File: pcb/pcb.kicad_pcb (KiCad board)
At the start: 2 copper layers, 63 x 56 mm, 70 parts, among them CN10 1x2, CN2 1x8, CN3 1x8, CN4 1x8, CN5 1x4, CN6 1x2, CN7 1x2, CN9 2x5, IC1 AP2112K-3.3TRG1, IC2 STM32f103C8T, IC3 INA199B2, IC4 AP62300TWU-7, IC5 MCP2551, SW1 switch_3x4, SW2 switch_3x4, SW3 219-3LPST, X1 H130B-8.000-18-3030-EXT-TR

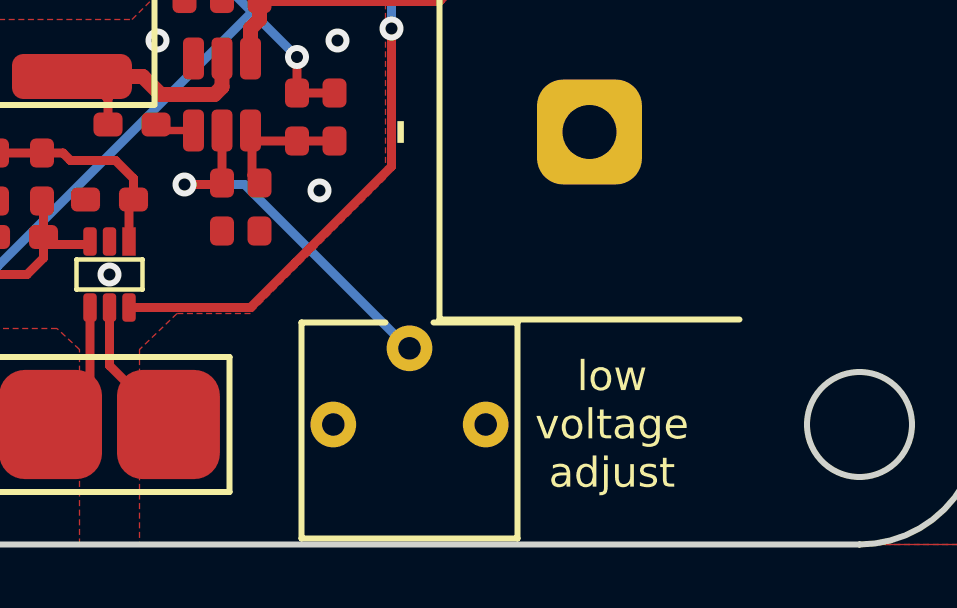
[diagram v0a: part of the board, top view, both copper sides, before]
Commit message: added resistor to tweak step-down low-voltage range. flipped trimmer polarity
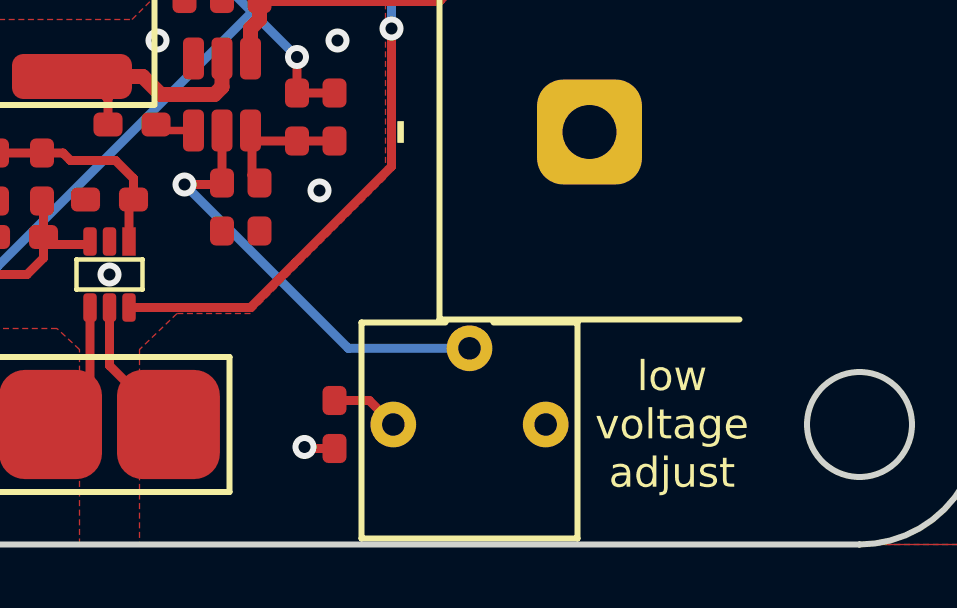
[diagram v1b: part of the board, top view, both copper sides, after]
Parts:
- added R17: 5k2, SMT:0603, F.Cu at (140.5, 126.0)
- moved R10 2.00 mm to (145.0, 126.0)
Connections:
- CN8 pad e: GND -> (no net)
- R10 pad 1: /Battery -> Net-(R10-Pad1)
- R10 pad 3: GND -> /Battery
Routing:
- net Net-(R10-Pad1): track 0.00 -> 2.29 mm
- net Net-(IC4-EN): track 12.8 -> 14.8 mm
- net GND: track 6.08 -> 7.10 mm, vias 37 -> 38
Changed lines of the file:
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@@
   (net 65 "unconnected-(IC2-OSC32_IN-Pad3)")
   (net 66 "unconnected-(IC2-OSC32_OUT-Pad4)")
+  (net 67 "Net-(R10-Pad1)")
   (footprint "pin_headers:1x2" (layer "F.Cu")
     (at 139.64 94.44)
@@
       (net 1 "GND") (pinfunction "SHLD") (pintype "power_out") (thermal_bridge_angle 45))
     (pad "e" smd roundrect (at 3.2 -4.755 270) (size 0.6 1.15) (layers "F.Cu" "F.Paste" "F.Mask") (roundrect_rratio 0.25)
-      (net 1 "GND") (pinfunction "GND") (pintype "power_out") (thermal_bridge_angle 0))
+      (thermal_bridge_angle 0))
     (model "USB4105-GF-A.stp"
       (offset (xyz 0 -2.5 0))
@@
   )
   (footprint "potentiometers:3362P" (layer "F.Cu")
-    (at 143 126)
+    (at 145 126)
     (property "DigiKey" "3362P-104LF-ND")
     (property "MPN" "3362P-1-104LF")
@@
       (stroke (width 0.1) (type default)) (fill none) (layer "F.Fab"))
     (pad "1" thru_hole circle (at -2.54 0) (size 1.524 1.524) (drill 0.75) (layers "*.Cu" "*.Mask")
-      (net 5 "/Battery") (pintype "bidirectional"))
+      (net 67 "Net-(R10-Pad1)") (pintype "bidirectional"))
     (pad "2" thru_hole circle (at 0 -2.54) (size 1.524 1.524) (drill 0.75) (layers "*.Cu" "*.Mask")
       (net 13 "Net-(IC4-EN)") (pintype "bidirectional"))
     (pad "3" thru_hole circle (at 2.54 0) (size 1.524 1.524) (drill 0.75) (layers "*.Cu" "*.Mask")
-      (net 1 "GND") (pintype "bidirectional"))
+      (net 5 "/Battery") (pintype "bidirectional"))
     (model ":KICAD7_3DMODEL_DIR:1x1x1.wrl"
       (offset (xyz 0 0 0))
@@
     )
   )
+  (footprint "SMT:0603" (layer "F.Cu")
+    (at 140.5 126 90)
+    (property "Sheetfile" "power-supply.kicad_sch")
+    (property "Sheetname" "power supply")
+    (property "Sim.Device" "R")
+    (property "Sim.Pins" "1=+ 2=-")
+    (attr through_hole)
+    (fp_text reference "R17" (at 0 1.5 90) (layer "F.SilkS") hide
+        (effects (font (size 1 1) (thickness 0.15)))
+    )
+    (fp_text value "5k2" (at 0 -1.5 90) (layer "F.Fab") hide
+        (effects (font (size 1 1) (thickness 0.15)))
+    )
+    (fp_line (start -0.8 -0.4) (end 0.8 -0.4)
+      (stroke (width 0.2) (type solid)) (layer "F.Fab"))
+    (fp_line (start -0.8 0.4) (end -0.8 -0.4)
+      (stroke (width 0.2) (type solid)) (layer "F.Fab"))
+    (fp_line (start -0.8 0.4) (end 0.8 0.4)
+      (stroke (width 0.2) (type solid)) (layer "F.Fab"))
+    (fp_line (start 0.8 0.4) (end 0.8 -0.4)
+      (stroke (width 0.2) (type solid)) (layer "F.Fab"))
+    (pad "1" smd roundrect (at -0.8 0 90) (size 0.97 0.8) (layers "F.Cu" "F.Paste" "F.Mask") (roundrect_rratio 0.25)
+      (net 1 "GND") (pintype "bidirectional"))
+    (pad "2" smd roundrect (at 0.8 0 90) (size 0.97 0.8) (layers "F.Cu" "F.Paste" "F.Mask") (roundrect_rratio 0.25)
+      (net 67 "Net-(R10-Pad1)") (pintype "bidirectional"))
+    (model "passive.wrl"
+      (offset (xyz 0 0 0))
+      (scale (xyz 1.6 0.8 0.45))
+      (rotate (xyz 0 0 0))
+    )
+  )
   (footprint "connectors:XT60" (layer "F.Cu")
     (at 115.425 114.5 -90)
@@
     (effects (font (size 2 2) (thickness 0.3)) (justify bottom))
   )
-  (gr_text "low\nvoltage\nadjust" (at 149.75 126) (layer "F.SilkS")
+  (gr_text "low\nvoltage\nadjust" (at 151.75 126) (layer "F.SilkS")
     (effects (font (size 1 1) (thickness 0.15)))
   )
@@
     (style (thickness 0.15) (arrow_length 1.27) (text_position_mode 0) (extension_height 0.58642) (extension_offset 0.5) keep_text_aligned)
   )
+  (segment (start 139.55 126.8) (end 139.5 126.75) (width 0.3) (layer "F.Cu") (net 1))
+  (segment (start 140.5 126.8) (end 139.55 126.8) (width 0.3) (layer "F.Cu") (net 1))
   (segment (start 115.75 87.3) (end 116.3 86.75) (width 0.3) (layer "F.Cu") (net 1))
   (segment (start 120.25 97.25) (end 120.25 98) (width 0.3) (layer "F.Cu") (net 1))
@@
   (via (at 133.4 90.6) (size 0.8) (drill 0.4) (layers "F.Cu" "B.Cu") (free) (net 1))
   (via (at 111.25 95.25) (size 0.8) (drill 0.4) (layers "F.Cu" "B.Cu") (free) (net 1))
+  (via (at 139.5 126.75) (size 0.8) (drill 0.4) (layers "F.Cu" "B.Cu") (net 1))
   (via (at 132 105.4) (size 0.8) (drill 0.4) (layers "F.Cu" "B.Cu") (free) (net 1))
   (via (at 115.3 94.1) (size 0.8) (drill 0.4) (layers "F.Cu" "B.Cu") (free) (net 1))
@@
   (segment (start 136.75 117.95) (end 136.75 116.2) (width 0.3) (layer "F.Cu") (net 13))
   (via (at 135.5 118) (size 0.8) (drill 0.4) (layers "F.Cu" "B.Cu") (net 13))
-  (segment (start 137.5 118) (end 142.96 123.46) (width 0.3) (layer "B.Cu") (net 13))
-  (segment (start 142.96 123.46) (end 143 123.46) (width 0.3) (layer "B.Cu") (net 13))
-  (segment (start 135.5 118) (end 137.5 118) (width 0.3) (layer "B.Cu") (net 13))
+  (segment (start 135.5 118) (end 140.96 123.46) (width 0.3) (layer "B.Cu") (net 13))
+  (segment (start 140.96 123.46) (end 145 123.46) (width 0.3) (layer "B.Cu") (net 13))
   (segment (start 118.25 97.25) (end 118.25 95.51) (width 0.3) (layer "F.Cu") (net 14))
   (segment (start 118.25 95.51) (end 119.32 94.44) (width 0.3) (layer "F.Cu") (net 14))
@@
   (segment (start 110.75 88) (end 105.25 88) (width 0.3) (layer "F.Cu") (net 61))
   (segment (start 105.25 88) (end 102.46 85.21) (width 0.3) (layer "F.Cu") (net 61))
+  (segment (start 140.5 125.2) (end 141.66 125.2) (width 0.3) (layer "F.Cu") (net 67))
+  (segment (start 141.66 125.2) (end 142.46 126) (width 0.3) (layer "F.Cu") (net 67))
   (zone (net 17) (net_name "/power supply/+") (layer "F.Cu") (hatch edge 0.5)
     (priority 2)

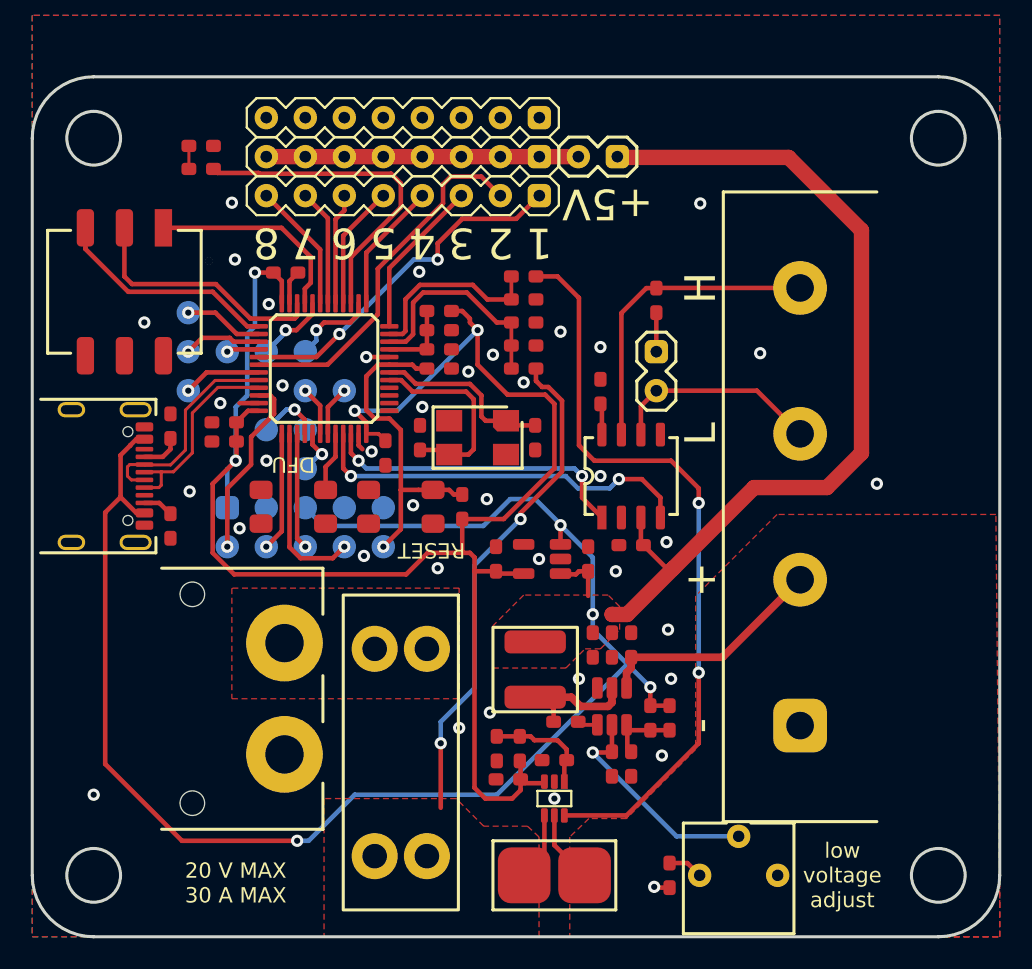
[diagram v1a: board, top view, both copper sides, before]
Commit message: minor tweaks on battery current paths
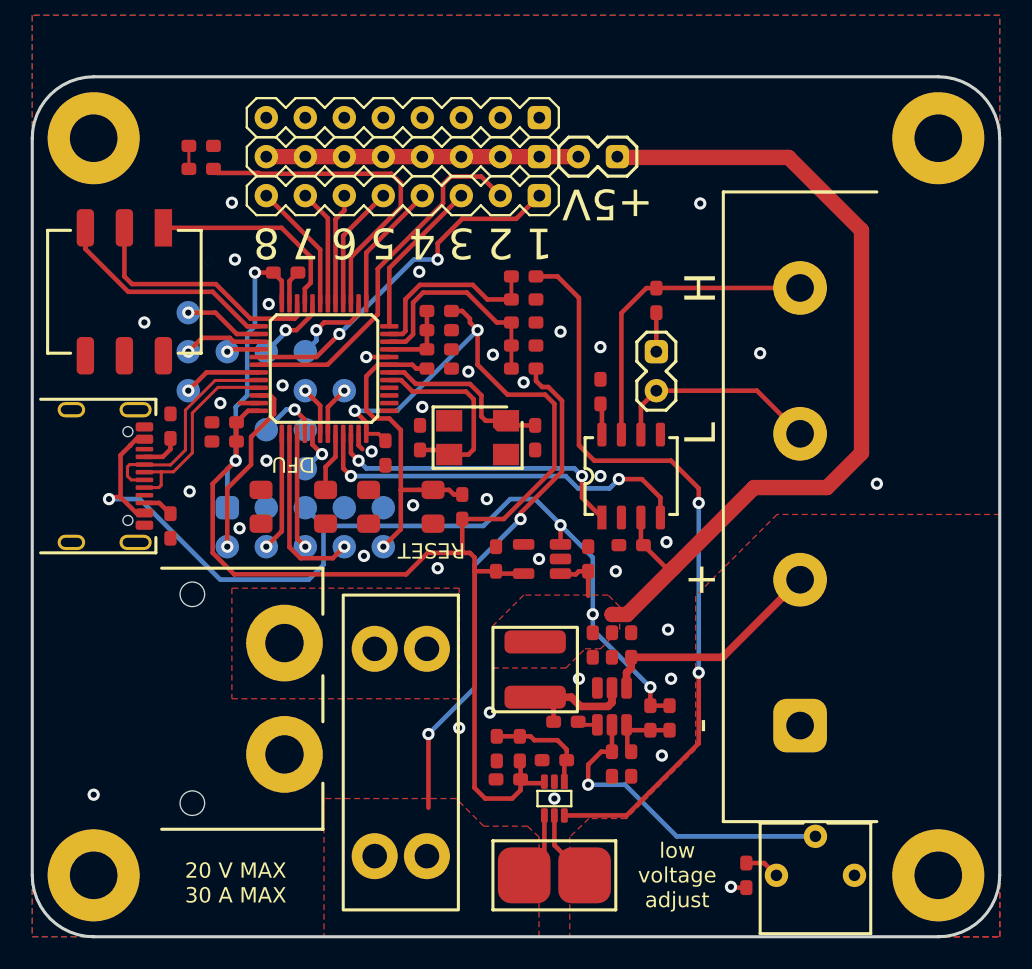
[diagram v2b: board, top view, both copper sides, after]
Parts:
- added REF**: M3, PCB:M3, F.Cu at (158.0, 126.0)
- added REF**: M3, PCB:M3, F.Cu at (103.0, 78.0)
- added REF**: M3, PCB:M3, F.Cu at (103.0, 126.0)
- added REF**: M3, PCB:M3, F.Cu at (158.0, 78.0)
- moved R10 5.00 mm to (150.0, 126.0)
- moved R17 5.00 mm to (145.5, 126.0)
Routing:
- net 5V: track 161.5 -> 122.8 mm
- net Net-(IC4-EN): track 14.8 -> 21.1 mm
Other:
- outline, holes or cut-outs redrawn

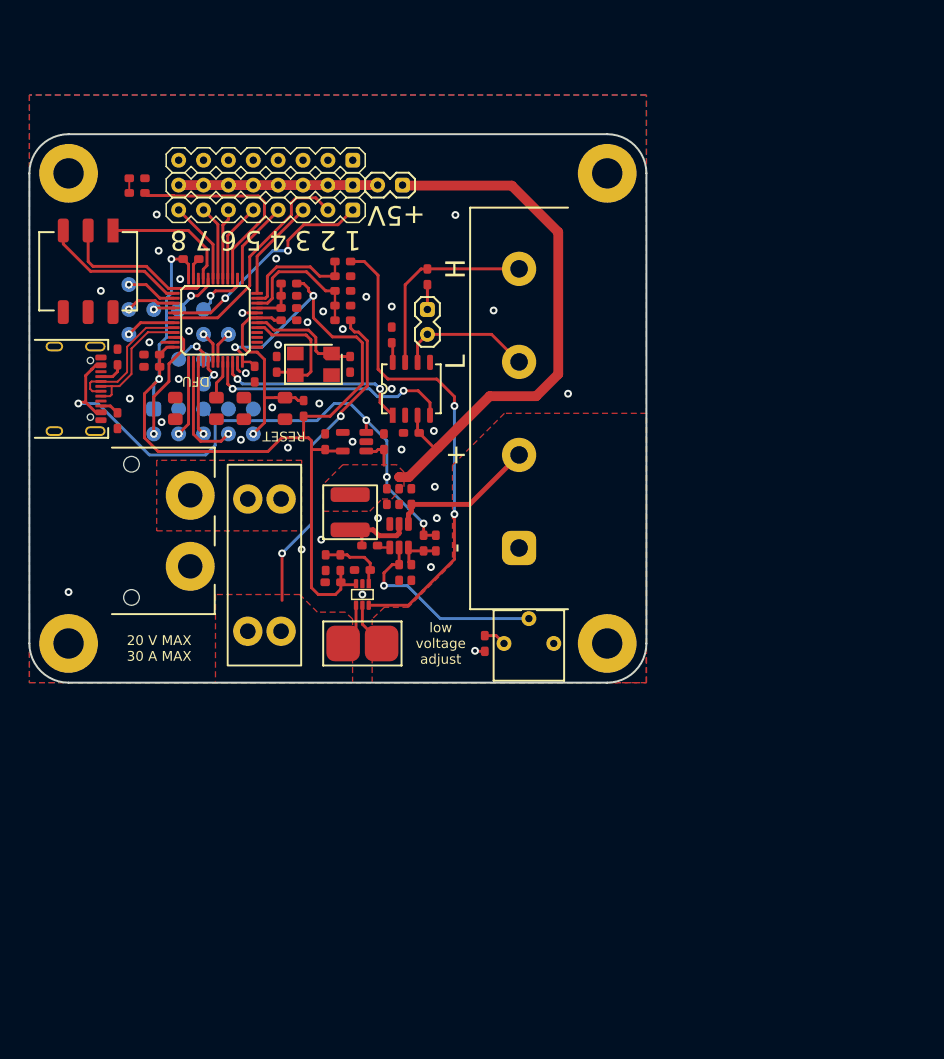
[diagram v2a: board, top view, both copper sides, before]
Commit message: changed output connector to xt60 & 2x jst-xh-4
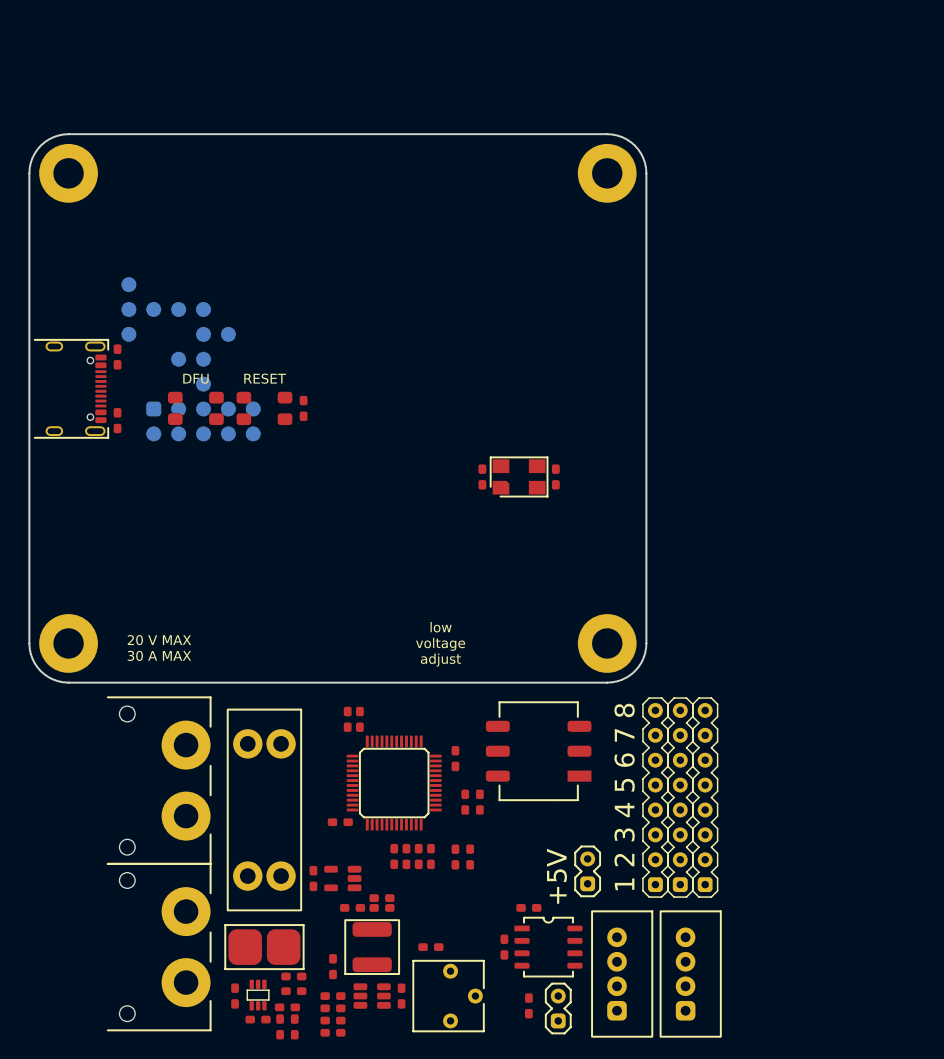
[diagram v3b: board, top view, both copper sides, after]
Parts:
- added CN1: 1x4, jst-xh:jst-xh-4, F.Cu at (166.0, 159.8)
- added CN11: 1x2, connectors:XT60, F.Cu at (115.0, 157.0)
- C13: value 4u7 -> 10u
- CN5: footprint connectors:YK4410403000G -> jst-xh:jst-xh-4
- R5: value 11k -> 10k
- R6: value 22k -> 20k
- R8: value 10k -> 8k2
- R9: value 56k2 -> 1k5
- moved CN4 79.4 mm to (168.0, 143.0), turned to 180 degrees
- moved CN3 75.9 mm to (165.5, 143.0), turned to 180 degrees
- moved R11 75.8 mm to (120.0, 162.0), turned to 90 degrees
- moved R14 75.2 mm to (150.0, 163.0)
- moved D1 72.7 mm to (145.0, 142.2), turned to -90 degrees
- moved CN2 72.4 mm to (162.9, 143.0), turned to 180 degrees
- moved CN7 72.1 mm to (156.0, 148.0), turned to 180 degrees
- moved R4 70.6 mm to (143.5, 142.2), turned to -90 degrees
- moved R1 70.2 mm to (126.0, 161.5), turned to 0 degrees
- moved CN10 68.9 mm to (153.0, 162.0), turned to 180 degrees
- moved SW3 67.2 mm to (151.0, 137.0), turned to 180 degrees
- moved R2 67.2 mm to (126.0, 160.0), turned to 180 degrees
- moved C22 60.7 mm to (144.0, 147.8), turned to -90 degrees
- moved R16 60.3 mm to (140.0, 147.8), turned to -90 degrees
- moved R15 60.2 mm to (150.0, 153.0), turned to 0 degrees
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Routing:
- net 5V: track 122.8 -> 0.00 mm, vias 4 -> 0
- net 3V3: track 111.6 -> 0.00 mm, vias 4 -> 0
- net Net-(IC3-OUT): track 49.2 -> 0.00 mm, vias 2 -> 0
- net /power supply/+: track 37.6 -> 0.00 mm, vias 2 -> 0
- net /CAN/CAN_RX: track 25.5 -> 0.00 mm, vias 2 -> 0
- net /MCU/CH2: track 23.8 -> 0.00 mm
- net /MCU/CH1: track 23.2 -> 0.00 mm, vias 2 -> 0
- net /MCU/status: track 21.7 -> 0.00 mm
- net /MCU/NRST: track 21.5 -> 0.00 mm, vias 1 -> 0
- net Net-(IC4-EN): track 21.1 -> 0.00 mm, vias 1 -> 0
- net /Servo VCC: track 20.3 -> 0.00 mm
- net /CAN_H: track 20.2 -> 0.00 mm
- net /CAN/CAN_TX: track 20.2 -> 0.00 mm, vias 2 -> 0
- net /Battery: track 19.9 -> 0.00 mm
- net /MCU/ADDR2: track 16.5 -> 0.00 mm
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- removed copper zone on F.Cu, net /Battery
- removed copper zone on F.Cu, net /power supply/+
- removed copper zone on F.Cu, net 5V
- removed copper zone on B.Cu, net GND
- removed copper zone on F.Cu, net GND
- removed copper zone on F.Cu, net Net-(CN6-Pad1)
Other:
- board text removed: "+"
- board text removed: "-"
- board text removed: "H"
- board text removed: "L"

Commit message: worked on layout
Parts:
- removed CN8: ~, USB:USB4105-GF-A
- removed R12, R13: 5k1, SMT:0603
- added TP10: test_point, PCB:test_point, B.Cu at (125.9, 90.4)
- added TP9: test_point, PCB:test_point, B.Cu at (128.4, 90.4)
- moved D1 58.5 mm to (123.3, 87.9), turned to 90 degrees
- moved R4 57.4 mm to (124.8, 87.9), turned to 90 degrees
- moved SW3 54.5 mm to (131.7, 86.0), turned to -90 degrees
- moved R1 50.9 mm to (120.0, 111.0), turned to -90 degrees
- moved R2 49.5 mm to (118.8, 111.0), turned to 90 degrees
- moved C8 49.4 mm to (123.6, 115.0)
- moved C25 49.4 mm to (123.6, 113.8)
- moved R5 49.0 mm to (123.6, 116.2), turned to 180 degrees
- moved CN2 48.9 mm to (143.6, 98.1)
- moved CN3 48.9 mm to (146.2, 98.1)
- moved CN4 48.9 mm to (148.7, 98.1)
- moved CN5 48.6 mm to (141.1, 114.6)
- moved C24 48.5 mm to (129.5, 112.0)
- moved IC5 48.4 mm to (134.1, 112.0)
- moved CN1 48.4 mm to (148.7, 114.6)
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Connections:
- CN10 pad 1: Net-(CN10-Pad1) -> /CAN_H
- CN10 pad 2: /CAN_L -> Net-(CN10-Pad2)
- IC2 pad 32: /MCU/USB_N -> Net-(IC2-PA11)
- IC2 pad 33: /MCU/USB_P -> Net-(IC2-PA12)
- R14 pad 1: Net-(CN10-Pad1) -> Net-(CN10-Pad2)
- R14 pad 2: /CAN_H -> /CAN_L
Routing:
- net Net-(IC4-BST): track 0.00 -> 8.30 mm, vias 0 -> 2
- net /power supply/+: track 0.00 -> 4.58 mm
- net /Battery: track 0.00 -> 4.58 mm
- net Net-(IC4-SW): track 0.00 -> 4.01 mm
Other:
- board size 63 x 56 mm -> 55 x 52.5 mm
- board text added: "fix via sizes"
- board text added: "locked"
- board text removed: "+5V"
- board text removed: "1"
- board text removed: "2"
- board text removed: "20 V MAX 30 A MAX"
- board text removed: "3"
- board text removed: "4"
- board text removed: "5"
- board text removed: "6"
- board text removed: "7"
- board text removed: "8"
- board text removed: "low voltage adjust"
